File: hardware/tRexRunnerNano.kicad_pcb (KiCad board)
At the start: 2 copper layers, 42 x 32 mm, 32 parts, among them IC1 TPS2112APWR, IC2 MAX1555EZK_T, IC3 TPS73033DBVR, IC4 CH32V003F4P6, J1 CHG, J2 BATT, J3 OLED, Q1 BC847, Q2 PNP, Q3 BC847, SW1 DUCK, SW2 JUMP

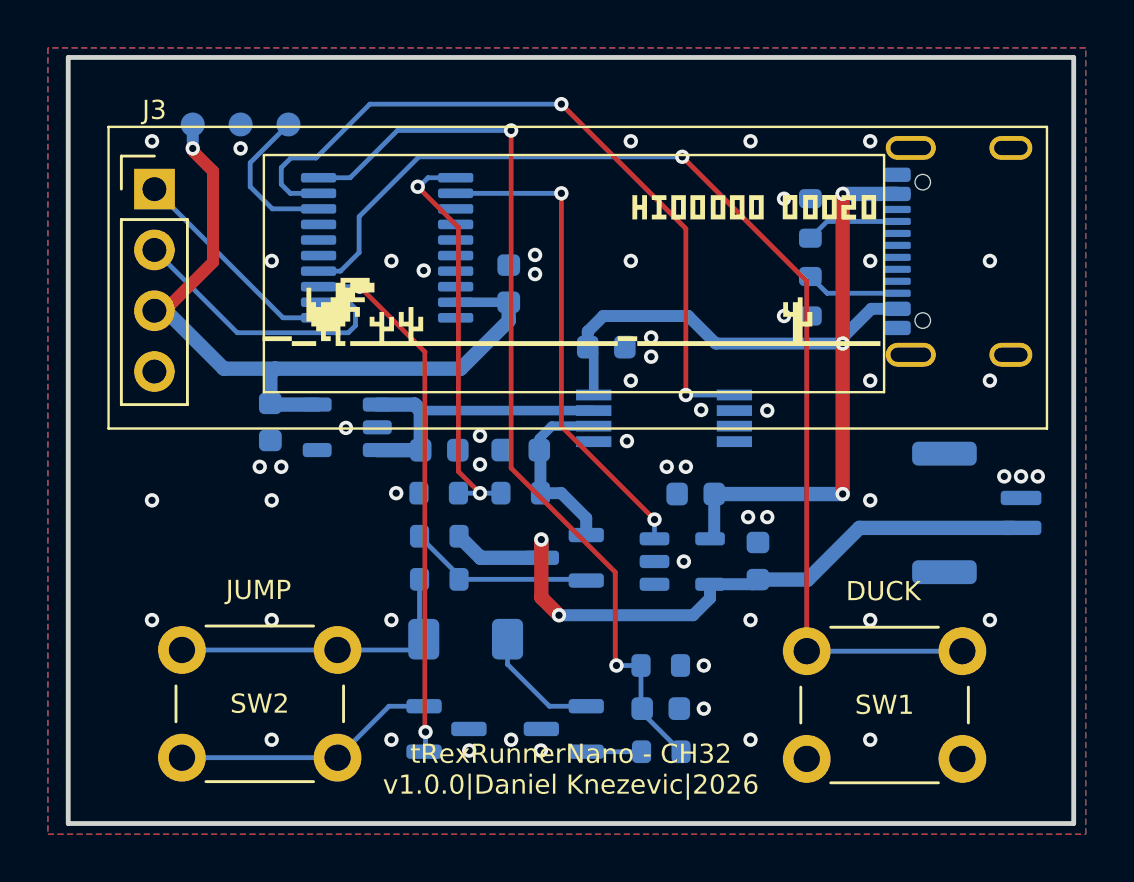
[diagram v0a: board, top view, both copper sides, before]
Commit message: Fix BC8x7 transistor pinouts and TPS2112A configuration
- Update PCB version to v1.0.1.
- Fix BC847 and BC857 footprints to match correct B-E-C layout.
- Connect TPS2112APWR VSNS pin to GND for proper mode selection.
- Add current-limiting resistor to TPS2112APWR ILIM pin.
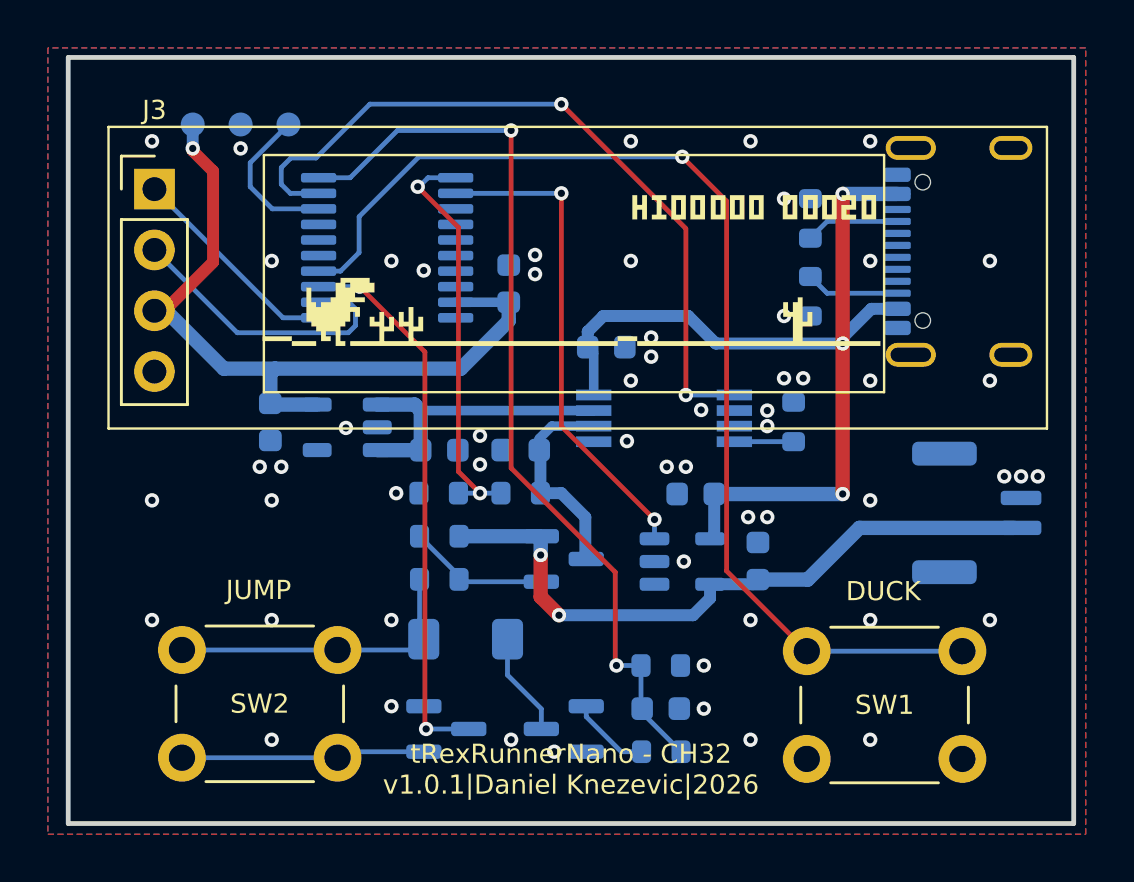
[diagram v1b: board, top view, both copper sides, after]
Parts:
- added R9: 470, Resistor_SMD:R_0603_1608Metric, B.Cu at (111.5, 58.0)
- J2: value BATT -> - BAT +
- Q2: value PNP -> BC857
- R5: value 330k -> 100k
- moved Q2 0.05 mm to (101.8, 63.8), turned to 0 degrees
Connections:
- IC1 pad 3: unconnected-(IC1-VSNS-Pad3) -> GND
- IC1 pad 4: unconnected-(IC1-ILIM-Pad4) -> Net-(IC1-ILIM)
- Q1 pad 1: Net-(D1-K) -> Net-(Q1-B)
- Q1 pad 2: Net-(Q1-B) -> GND
- Q1 pad 3: GND -> Net-(D1-K)
- Q2 pad 1: VDD -> Net-(Q2-B)
- Q2 pad 2: Net-(Q2-B) -> +BATT
- Q2 pad 3: +BATT -> VDD
- Q3 pad 1: /JUMP_BTN -> Net-(Q3-B)
- Q3 pad 2: Net-(Q3-B) -> GND
- Q3 pad 3: GND -> /JUMP_BTN
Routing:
- net Net-(IC1-ILIM): track 0.00 -> 2.47 mm
- net Net-(Q2-B): track 7.82 -> 5.88 mm
- net Net-(Q1-B): track 2.25 -> 3.36 mm
- net +BATT: track 29.2 -> 28.2 mm
- net VDD: track 7.89 -> 8.83 mm
- net Net-(Q3-B): track 11.1 -> 10.2 mm
- net /JUMP_BTN: track 22.3 -> 23.1 mm
- net Net-(D1-K): track 5.12 -> 4.34 mm
- net GND: vias 55 -> 57
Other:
- board text added: "tRexRunnerNano - CH32 v1.0.1|Daniel Knezevic|2026"
- board text removed: "tRexRunnerNano - CH32 v1.0.0|Daniel Knezevic|2026"
